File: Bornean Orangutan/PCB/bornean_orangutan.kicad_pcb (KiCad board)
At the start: 2 copper layers, 95.2 x 95.2 mm, 68 parts, among them J1 TRRS, J2 TRRS, SW1 SW_Push, U1 ATmega32U4-AU, Y1 16MHz

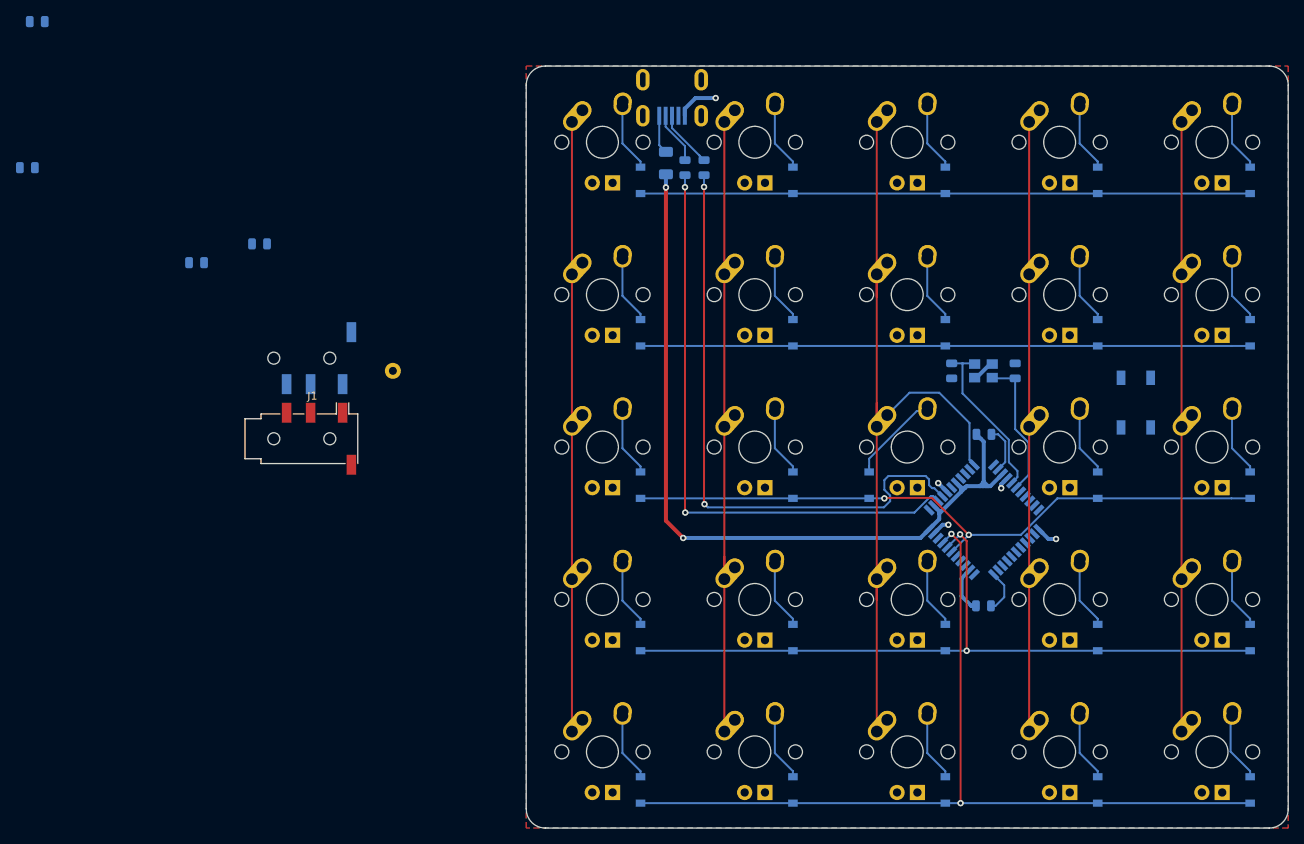
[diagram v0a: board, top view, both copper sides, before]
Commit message: Delete Tracks on Bornean Orangutan-PCB
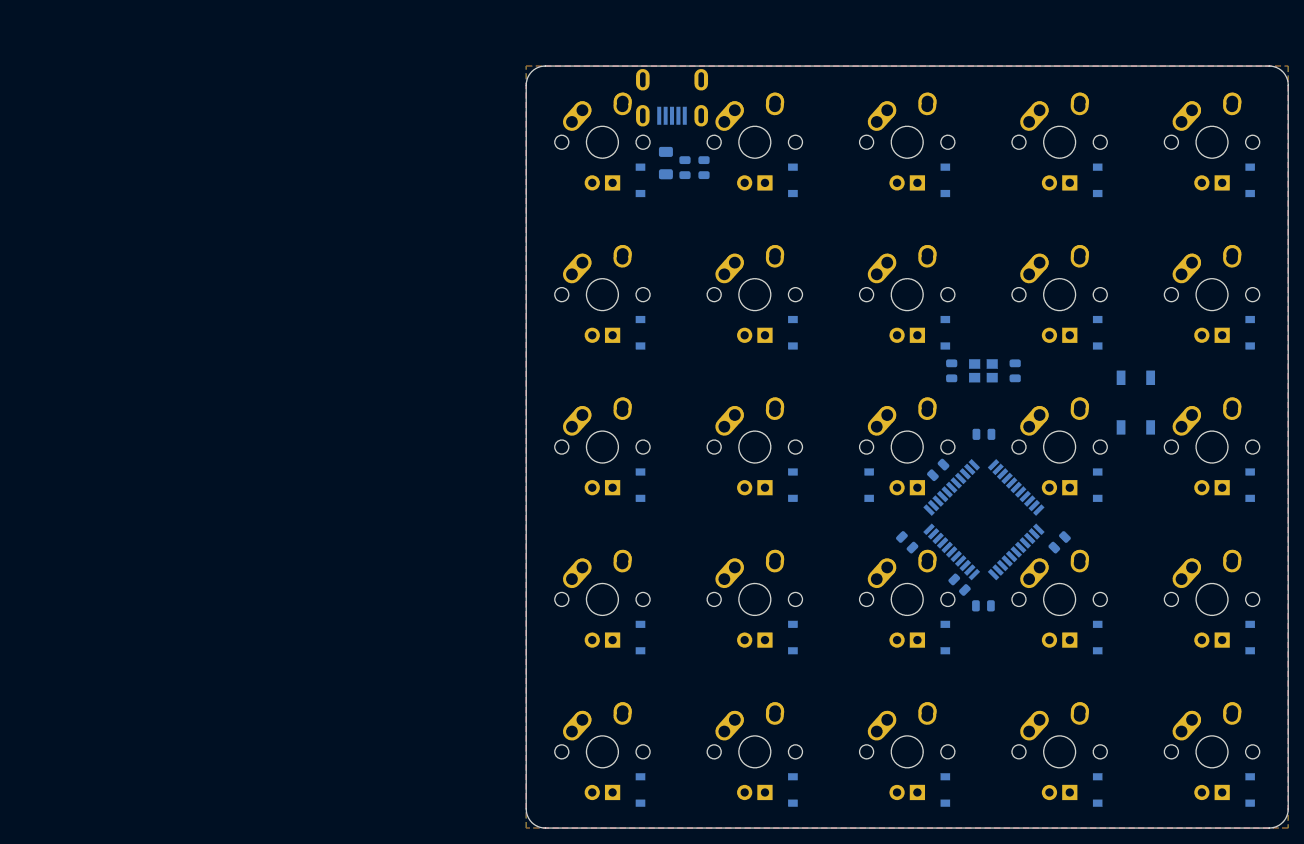
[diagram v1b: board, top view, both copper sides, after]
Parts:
- removed EXTRADATA1: Extradata, Connector_Pin:Pin_D1.0mm_L10.0mm
- removed J1, J2: TRRS, Connector_Audio:Jack_3.5mm_PJ320D_Horizontal
- moved C4 137.3 mm to (185.7, 115.1), turned to 45 degrees
- moved C5 126.7 mm to (166.7, 115.1), turned to 315 degrees
- moved C3 103.5 mm to (173.2, 120.4), turned to 135 degrees
- moved C6 89.4 mm to (170.6, 106.0), turned to 225 degrees
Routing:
- net ROW4: track 111.9 -> 0.00 mm, vias 2 -> 0
- net COL2: track 104.9 -> 0.00 mm
- net +5V: track 102.2 -> 0.00 mm, vias 2 -> 0
- net ROW3: track 93.4 -> 0.00 mm, vias 2 -> 0
- net ROW2: track 83.0 -> 0.00 mm, vias 2 -> 0
- net COL0: track 79.2 -> 0.00 mm
- net COL1: track 79.0 -> 0.00 mm
- net Net-(R2-Pad1): track 76.7 -> 0.00 mm, vias 2 -> 0
- net ROW1: track 76.2 -> 0.00 mm
- net ROW0: track 76.2 -> 0.00 mm
- net COL4: track 76.2 -> 0.00 mm
- net COL3: track 76.2 -> 0.00 mm
- net Net-(R3-Pad1): track 74.9 -> 0.00 mm, vias 2 -> 0
- net GND: track 22.3 -> 0.00 mm, vias 5 -> 0
- net Net-(C2-Pad1): track 21.0 -> 0.00 mm
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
